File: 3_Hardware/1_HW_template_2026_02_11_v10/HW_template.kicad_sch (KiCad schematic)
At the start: 5 parts, among them P1 ${SIM.PARAMS}, P2 ${SIM.PARAMS}

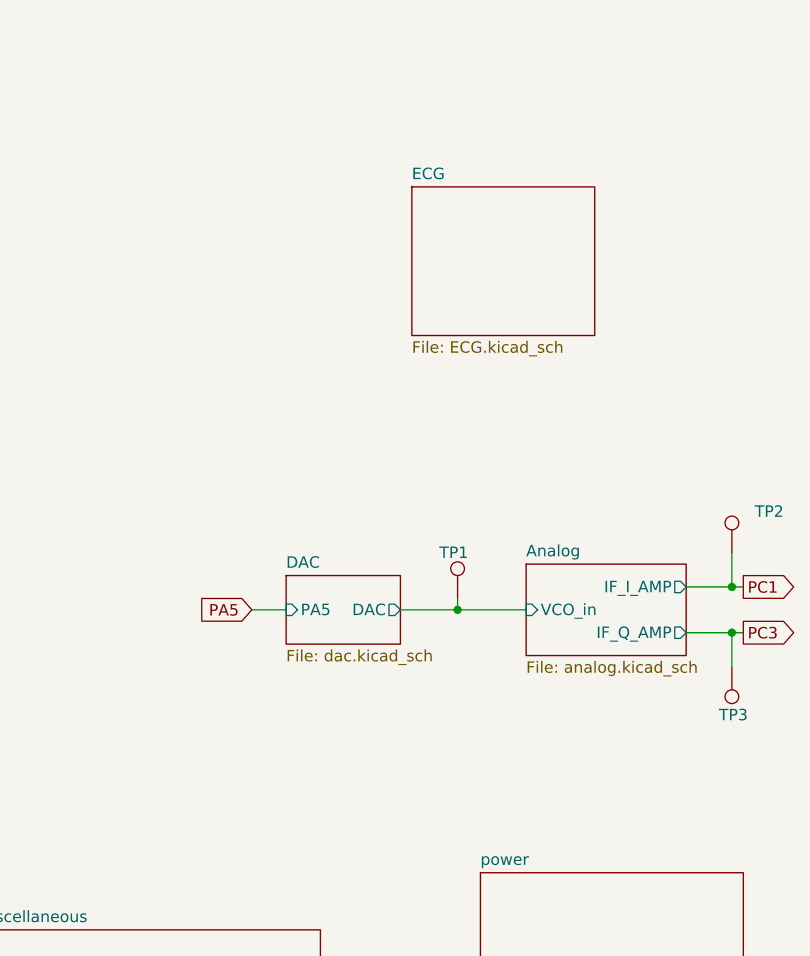
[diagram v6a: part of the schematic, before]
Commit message: updated layout
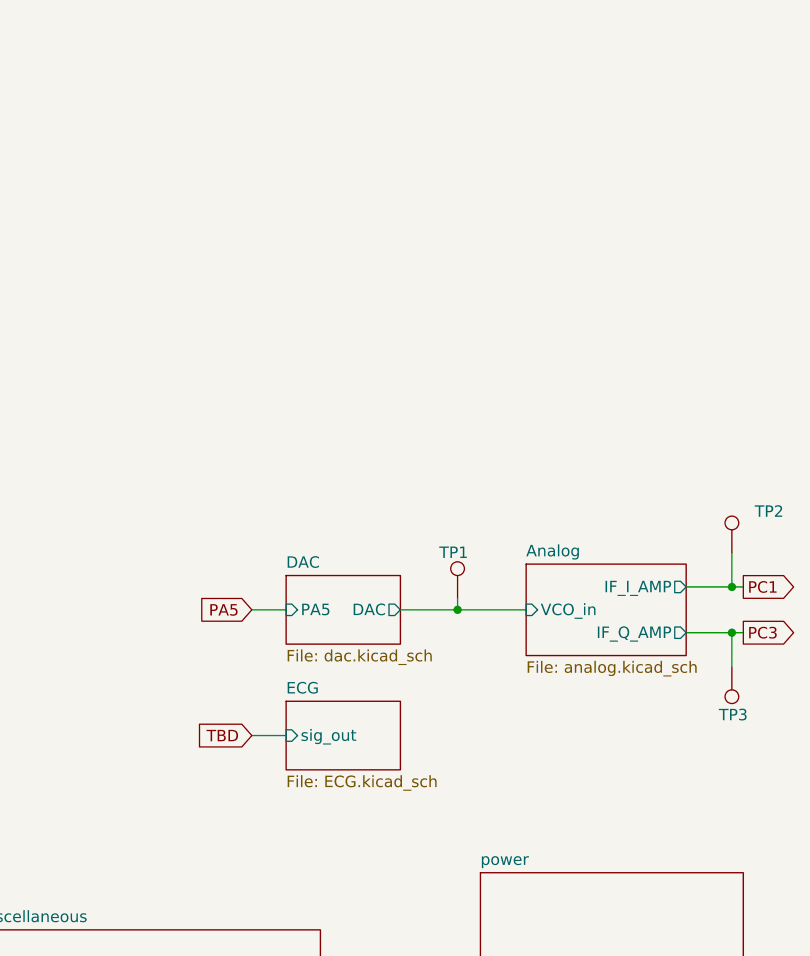
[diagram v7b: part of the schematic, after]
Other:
- sheet ECG ports: added sig_out; removed none
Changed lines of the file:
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@@
+	(wire
+		(pts
+			(xy 140.97 105.41) (xy 144.78 105.41)
+		)
+		(stroke
+			(width 0)
+			(type default)
+		)
+	)
 	(wire
 		(pts
@@
 				)
 				(justify left)
+				(hide yes)
+			)
+		)
+	)
+	(global_label "TBD"
+		(shape input)
+		(at 140.97 105.41 180)
+		(fields_autoplaced yes)
+		(effects
+			(font
+				(size 1.27 1.27)
+			)
+			(justify right)
+		)
+		(property "Intersheetrefs" "${INTERSHEET_REFS}"
+			(at 134.4772 105.41 0)
+			(effects
+				(font
+					(size 1.27 1.27)
+				)
+				(justify right)
 				(hide yes)
 			)
@@
 	)
 	(sheet
-		(at 158.75 44.45)
-		(size 20.32 16.51)
+		(at 144.78 101.6)
+		(size 12.7 7.62)
 		(exclude_from_sim no)
 		(in_bom yes)
@@
 		)
 		(property "Sheetname" "ECG"
-			(at 158.75 43.7384 0)
+			(at 144.78 100.8884 0)
 			(effects
 				(font
@@
 		)
 		(property "Sheetfile" "ECG.kicad_sch"
-			(at 158.75 61.5446 0)
+			(at 144.78 109.8046 0)
 			(effects
 				(font
@@
 			)
 		)
+		(pin "sig_out" input
+			(at 144.78 105.41 180)
+			(effects
+				(font
+					(size 1.27 1.27)
+				)
+				(justify left)
+			)
+		)

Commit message: pcb schematics finished + layout
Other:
- note added: "PA5 = DAC_OUT2 = VCO input control"
- note added: "PC1 = ADC123_IN11 = channel I"
- note added: "PC3 = ADC123_IN13 = channel Q"
- note added: "PE3 = LED D1"
- note added: "PE5 = LED D0"
- note added: "PF6 = ADC3_IN4 = ECG output"
- note added: "PG14 = USART6_TX (+LED) = OpenLog RXI"
- note removed: "TO BE CONNECTED TO STM"
- moved on the sheet: P2, TP1, TP2, TP3
